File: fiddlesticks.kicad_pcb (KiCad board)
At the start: 4 copper layers, 50 x 50 mm, 99 parts, among them J1 Conn_01x02_Pin, J2 Conn_01x04_Pin, J3 Conn_01x04, J4 USB_C_Receptacle_USB2.0_16P, J5 Conn_02x04_Counter_Clockwise, J6 Conn_01x05_Pin, M1 Motor_DC, M2 Motor_DC, M3 Motor_DC, M4 Motor_DC, Q1 AO3400A, Q2 AO3400A, Q3 AO3400A, Q4 AO3400A, SW1 SW_Push, SW2 SW_Push, U1 MCP1640Bx-xCHY, U2 STM32F411CEUx, U3 SPX3819M5-L-3-3, U4 USBLC6-2SC6, U5 ICM-45605, Y1 8MHz 12pF

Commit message: routed some more things
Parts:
- removed C28: 10u, Capacitor_SMD:C_0805_2012Metric_Pad1.18x1.45mm_HandSolder
- C30, C32, C33, D10, D11, D13: moved to B.Cu
- moved D13 91.1 mm to (145.5, 125.5), turned to 90 degrees
- moved Y1 84.3 mm to (118.0, 103.0), turned to 90 degrees
- moved C11 83.4 mm to (121.0, 102.8), turned to 90 degrees
- moved C13 83.1 mm to (121.0, 106.6), turned to 90 degrees
- moved D11 82.1 mm to (134.0, 125.5), turned to 90 degrees
- moved C26 77.4 mm to (138.5, 112.5), turned to 90 degrees
- moved C33 76.5 mm to (138.5, 125.0), turned to 90 degrees
- moved D10 73.6 mm to (122.0, 125.5), turned to 90 degrees
- moved C32 66.9 mm to (127.0, 125.0), turned to 90 degrees
- moved C27 66.9 mm to (136.5, 112.6), turned to 90 degrees
- moved C29 65.3 mm to (134.6, 115.5)
- moved U5 59.4 mm to (133.8, 113.1)
- moved C30 59.3 mm to (115.0, 125.0), turned to 90 degrees
- moved R17 55.9 mm to (133.1, 109.7)
- moved C34 52.0 mm to (123.5, 118.5), turned to 90 degrees
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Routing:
- net GND: track 8.46 -> 52.3 mm, vias 17 -> 33
- net VBAT: track 13.0 -> 36.3 mm, vias 6 -> 3
- net /motor_driver_imu/PWM1: track 0.00 -> 21.2 mm, vias 0 -> 1
- net Net-(D11-A): track 0.00 -> 10.8 mm
- net Net-(D13-A): track 0.00 -> 10.7 mm
- net Net-(D10-A): track 0.00 -> 10.7 mm
- net /motor_driver_imu/PWM2: track 0.00 -> 9.72 mm, vias 0 -> 1
- net /motor_driver_imu/PWM3: track 0.00 -> 8.86 mm, vias 0 -> 1
- net /HSE_IN: track 0.00 -> 8.32 mm
- net /IMU_MOSI: track 0.00 -> 7.31 mm
- net /IMU_MISO: track 0.00 -> 7.06 mm, vias 0 -> 2
- net /IMU_CS: track 0.00 -> 6.82 mm, vias 0 -> 2
- net /HSE_OUT: track 0.00 -> 6.05 mm
- net +3.3V: track 0.00 -> 5.35 mm
- net Net-(Q1-G): track 0.43 -> 4.25 mm
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
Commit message: finished routing
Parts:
- removed C23, C6, C7, C8, C9: 10u, Capacitor_SMD:C_0805_2012Metric_Pad1.18x1.45mm_HandSolder
- removed J3: Conn_01x04, Connector_Wire:SolderWire-6sqmm_1x04_P14mm_D3.5mm_OD7mm
- removed J5: Conn_02x04_Counter_Clockwise, Connector_PinSocket_2.54mm:PinSocket_2x04_P2.54mm_Vertical
- removed U5: ICM-45605, IMU:XDCR_ICM-45605
- added MT1: ICM-42670-P, IMU:XDCR_ICM-42670-P, F.Cu at (135.0, 119.0)
- added TP5: TestPoint, TestPoint:TestPoint_Pad_1.5x1.5mm, F.Cu at (107.5, 100.5)
- added TP6: TestPoint, TestPoint:TestPoint_Pad_1.5x1.5mm, B.Cu at (107.5, 100.5)
- added TP7: TestPoint, TestPoint:TestPoint_Pad_1.5x1.5mm, F.Cu at (145.0, 118.0)
- C10, C12, C14, C15, C16, C18, C19, C24, C25, C4, D15, D16, D6, D7, D8, FB1, L1, R1, R12, R2, R3, R4, R5, R6, R7, R9, TP1, TP2, U1, U3: moved to B.Cu
- C21: value 100n -> 10uF; footprint Capacitor_SMD:C_0603_1608Metric_Pad1.08x0.95mm_HandSolder -> Capacitor_SMD:C_0805_2012Metric_Pad1.18x1.45mm_HandSolder; moved to B.Cu
- C22: value 100n -> 100nF; moved to B.Cu
- C26: value 10u -> 2.2uF
- C29: value 100n -> 10nF
- J4: value USB_C_Receptacle_USB2.0_16P -> TYPE-C-31-M-12; footprint Connector_USB:USB_C_Receptacle_Palconn_UTC16-G -> USB_CUSTOM:HRO_TYPE-C-31-M-12
- SW1: footprint coolswitch:XUNPU TS-1088-AR02016 -> coolswitch:SW_TS-1088-AR02016; moved to B.Cu
- SW2: footprint coolswitch:XUNPU TS-1088-AR02016 -> coolswitch:SW_TS-1088-AR02016
- moved SW2 100.7 mm to (138.1, 96.0), turned to 180 degrees
- moved C2 93.7 mm to (132.6, 100.0)
- moved D2 91.6 mm to (137.8, 93.5)
- moved C5 90.9 mm to (130.0, 111.6), turned to -90 degrees
- moved C3 84.7 mm to (123.4, 99.5), turned to 180 degrees
- moved C4 84.0 mm to (122.5, 100.9), turned to 90 degrees
- moved C10 83.8 mm to (122.9, 113.0)
- moved C16 82.7 mm to (126.1, 111.5), turned to 180 degrees
- moved R2 82.5 mm to (129.0, 96.1), turned to 90 degrees
- moved C25 81.1 mm to (123.5, 105.4), turned to 90 degrees
- moved D3 79.3 mm to (131.3, 124.5)
- moved D9 77.3 mm to (142.0, 115.4), turned to 90 degrees
- moved R1 77.1 mm to (124.9, 109.0), turned to 180 degrees
- moved R6 76.1 mm to (123.6, 114.5)
- moved R9 75.5 mm to (127.4, 105.1), turned to -90 degrees
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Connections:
- R17 pad 1: /IMU_SCK -> Net-(D12-K)
- R17 pad 2: Net-(D12-K) -> /IMU_SCK
- U2 pad 42: TIM4_CH1 -> unconnected-(U2-PB6-Pad42)
- U2 pad 43: TIM4_CH2 -> unconnected-(U2-PB7-Pad43)
- U2 pad 45: TIM4_CH3 -> unconnected-(U2-PB8-Pad45)
- U2 pad 46: TIM4_CH4 -> unconnected-(U2-PB9-Pad46)
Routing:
- net GND: track 52.3 -> 129.1 mm, vias 33 -> 64
- net /RC_RX: track 0.00 -> 60.4 mm, vias 0 -> 1
- net VBUS: track 15.2 -> 72.5 mm, vias 0 -> 1
- net /SWCLK: track 0.00 -> 53.4 mm, vias 0 -> 2
- net Net-(D6-K): track 0.00 -> 51.6 mm, vias 0 -> 1
- net +3.3V: track 5.35 -> 55.8 mm, vias 0 -> 12
- net /RC_TX: track 0.00 -> 49.0 mm, vias 0 -> 1
- net /motor_driver_imu/PWM2: track 9.72 -> 43.5 mm, vias 1 -> 3
- net /motor_driver_imu/PWM1: track 21.2 -> 53.0 mm, vias 1 -> 3
- net VBAT: track 36.3 -> 68.0 mm, vias 3 -> 5
- net /SWDIO: track 0.00 -> 31.6 mm, vias 0 -> 2
- net /motor_driver_imu/PWM4: track 0.00 -> 30.2 mm, vias 0 -> 1
- net +5V: track 0.00 -> 25.2 mm, vias 0 -> 3
- net VSYS: track 0.00 -> 22.4 mm, vias 0 -> 2
- net /mcu_boot0: track 0.00 -> 19.0 mm, vias 0 -> 2
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- added copper zone on In2.Cu, net +3.3V
- added copper zone on B.Cu, net GND
- added copper zone on In2.Cu, net VSYS
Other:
- board text added: "+ -"
- board text added: "3.3V"
- board text added: "5V"
- board text added: "BOOT0"
- board text added: "FIDDLESTICKS"
- board text added: "GND"
- board text added: "GND|3v3|5|RX|TX"
- board text added: "NRST"
- board text added: "RHR"
- board text added: "RX"
- board text added: "V0"
- board text added: "VBUS"
- board text added: "VBUS|VBAT"
- board text added: "VSYS"
- board text added: "X"
- board text added: "Y"

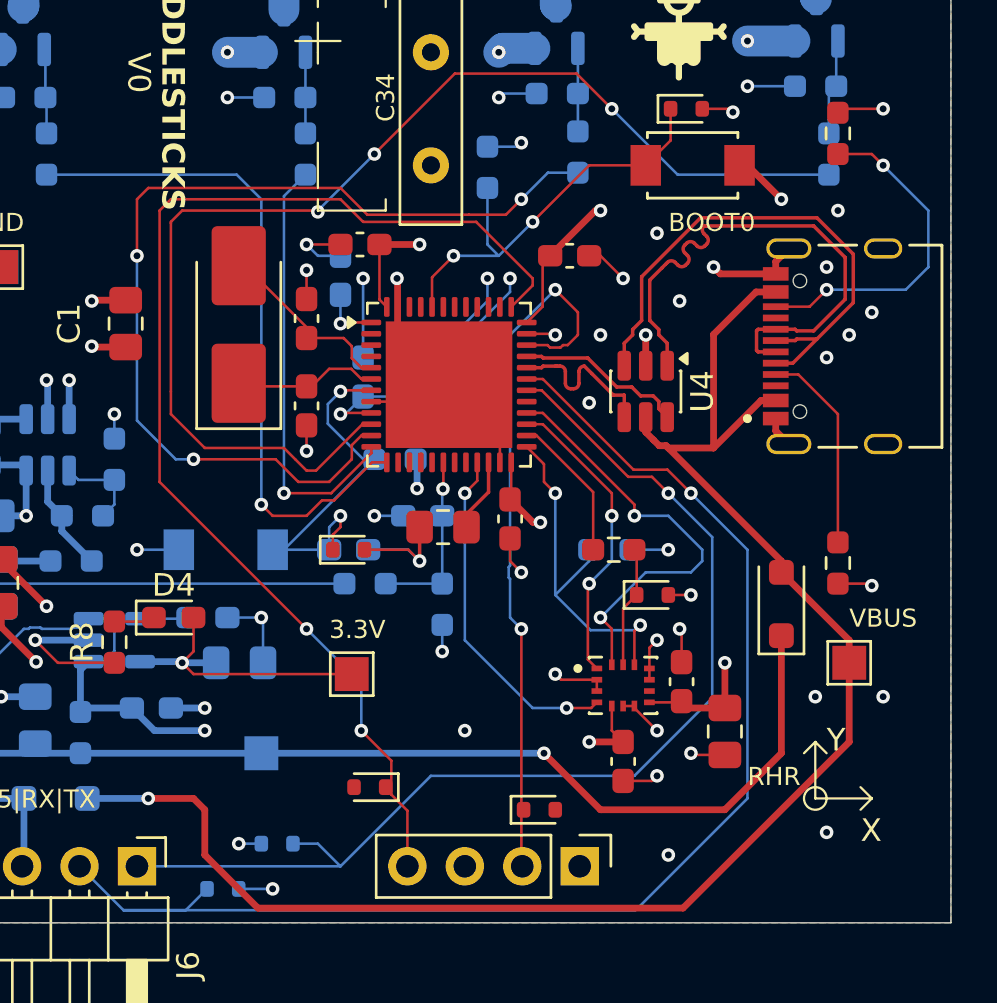
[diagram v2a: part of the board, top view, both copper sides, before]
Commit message: fixed usb routing, and esd/pull ups/pull downs placement
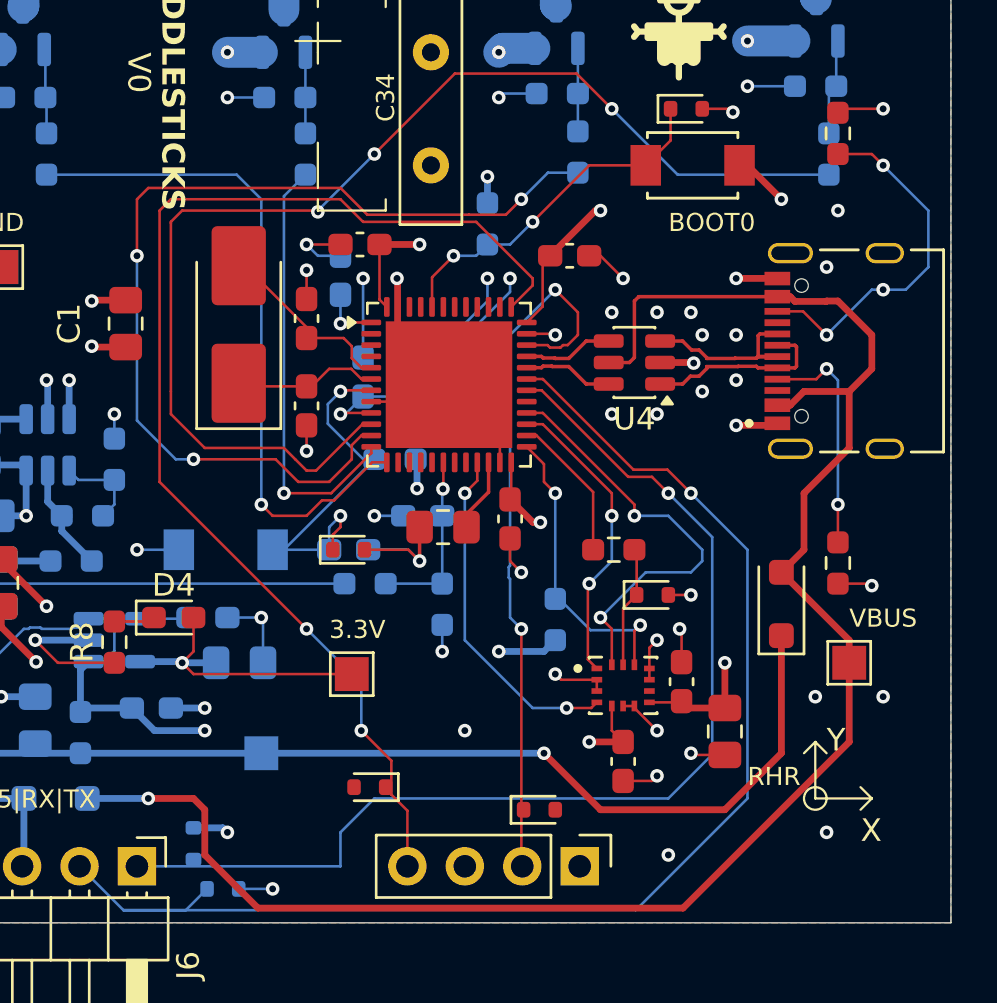
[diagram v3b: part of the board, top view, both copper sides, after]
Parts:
- moved R12 3.92 mm to (132.0, 116.1), turned to -90 degrees
- moved D15 3.70 mm to (116.0, 126.0), turned to 90 degrees
- moved R2 2.50 mm to (129.0, 98.6)
- moved U4 1.37 mm to (135.5, 104.7), turned to 180 degrees
- moved J4 0.22 mm to (146.6, 104.2)
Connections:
- U4 pad 1: /DIN+ -> /DIN-
- U4 pad 3: /DIN- -> /DIN+
- U4 pad 4: /USB_FS_D- -> /USB_FS_D+
- U4 pad 6: /USB_FS_D+ -> /USB_FS_D-
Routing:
- net /DIN+: track 24.2 -> 8.20 mm
- net /DIN-: track 23.9 -> 8.20 mm
- net VBUS: track 72.5 -> 79.3 mm
- net /USB_FS_D+: track 7.51 -> 3.98 mm
- net /USB_FS_D-: track 7.40 -> 3.98 mm
- net /mcu_boot0: track 19.0 -> 15.8 mm
- net /IMU_CS: track 16.0 -> 13.4 mm
- net GND: track 129.1 -> 127.5 mm, vias 64 -> 67
- net Net-(J4-CC1): track 9.15 -> 10.3 mm, vias 0 -> 2
- net +3.3V: track 55.8 -> 56.8 mm
- net Net-(J4-CC2): track 15.0 -> 15.9 mm, vias 2 -> 3

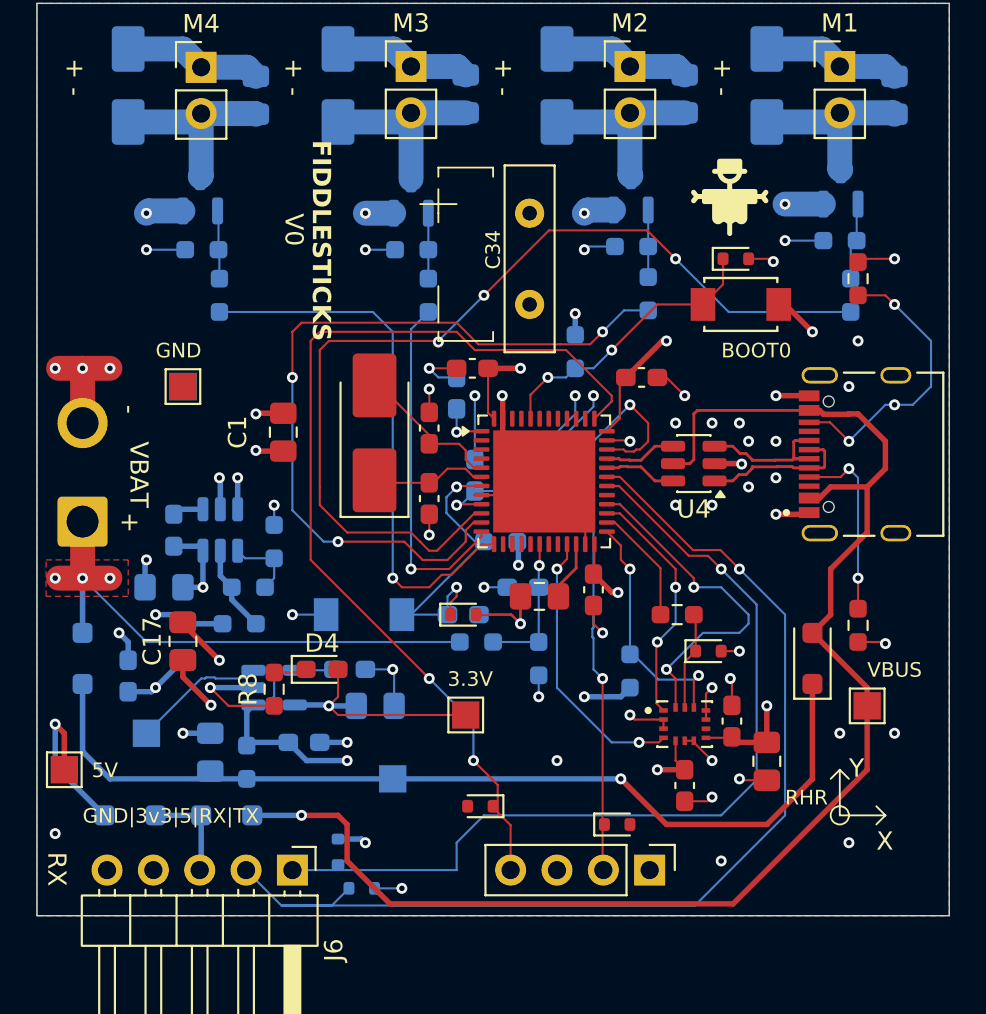
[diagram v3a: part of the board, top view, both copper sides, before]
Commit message: added vias under MCU, added silk screen for SWD
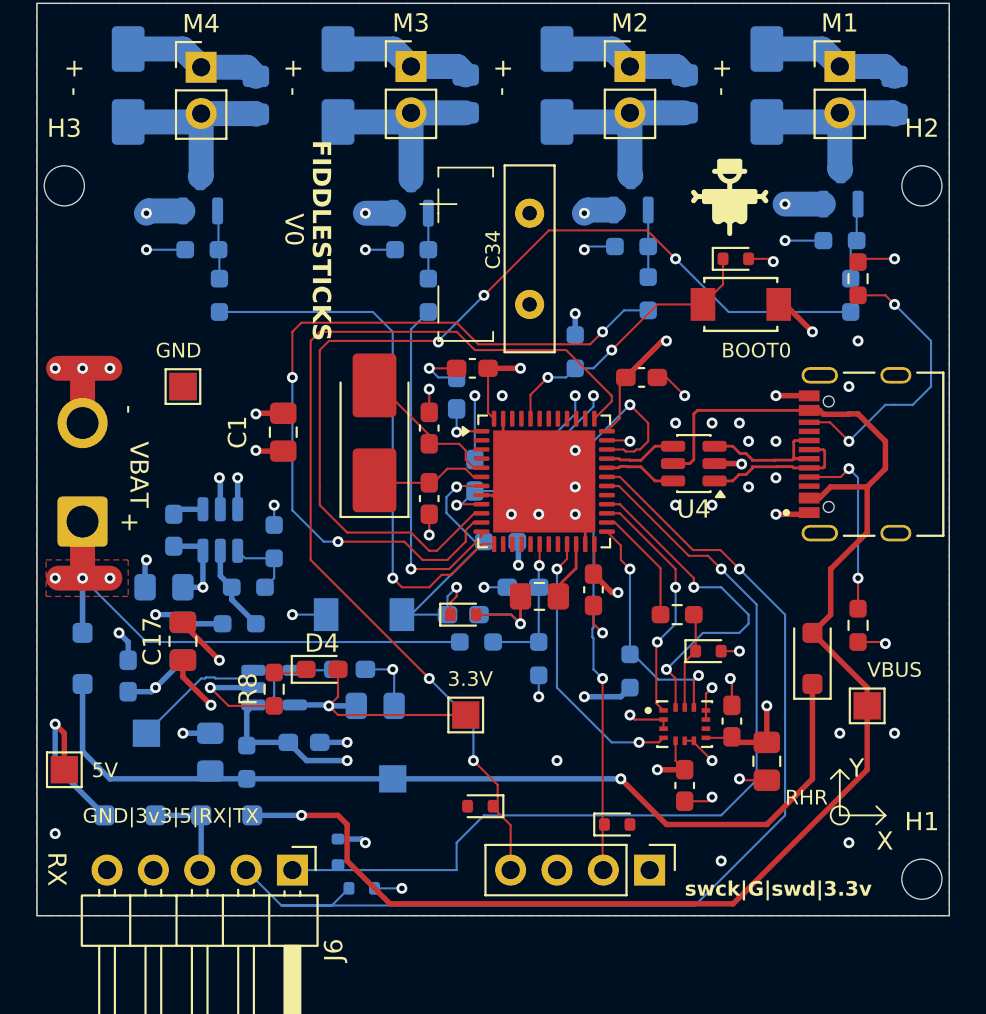
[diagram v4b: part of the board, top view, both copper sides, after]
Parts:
- added H1: MountingHole, MountingHole:MountingHole_2.2mm_M2, F.Cu at (148.0, 127.5)
- added H2: MountingHole, MountingHole:MountingHole_2.2mm_M2, F.Cu at (148.0, 89.5)
- added H3: MountingHole, MountingHole:MountingHole_2.2mm_M2, F.Cu at (101.0, 89.5)
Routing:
- net GND: track 127.5 -> 132.6 mm, vias 67 -> 72
- net Net-(J4-CC2): vias 3 -> 2
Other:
- board text added: "swck|G|swd|3.3v"

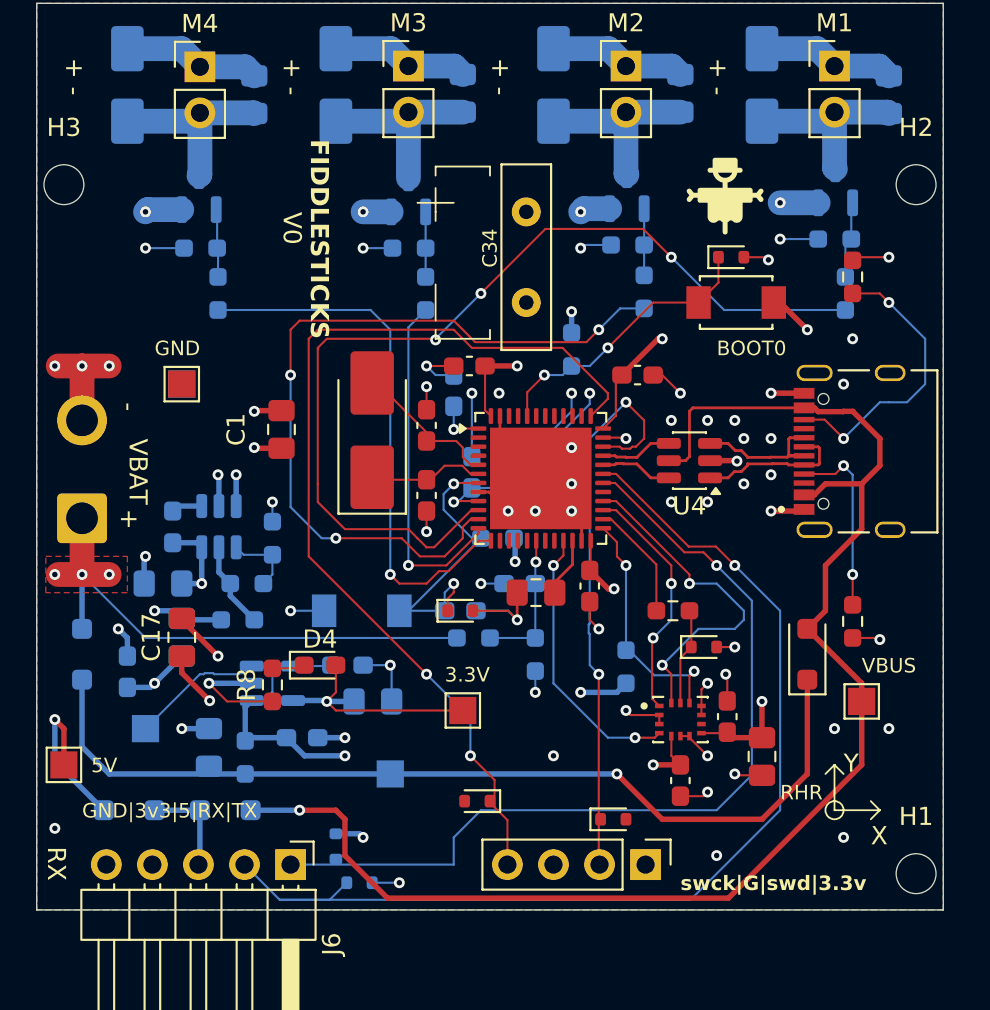
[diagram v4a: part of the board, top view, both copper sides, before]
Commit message: fixed some more routing
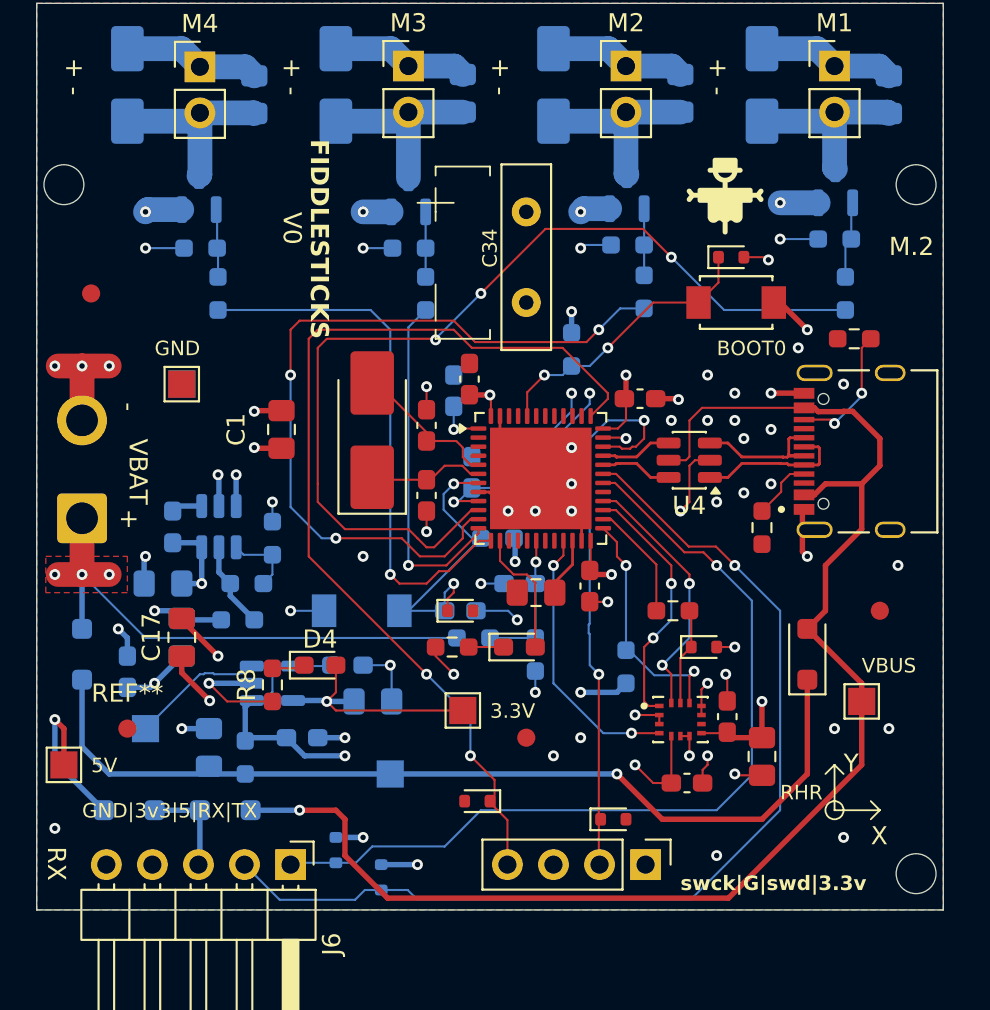
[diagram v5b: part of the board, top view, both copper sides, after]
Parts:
- added D14: GREEN, LED_SMD:LED_0603_1608Metric_Pad1.05x0.95mm_HandSolder, F.Cu at (126.1, 115.0)
- added R22: 1k, Resistor_SMD:R_0603_1608Metric_Pad0.98x0.95mm_HandSolder, F.Cu at (122.4, 115.0)
- added REF**: Fiducial_1mm_Mask2mm, Fiducial:Fiducial_1mm_Mask2mm, F.Cu at (146.0, 113.0)
- added REF**: Fiducial_1mm_Mask2mm, Fiducial:Fiducial_1mm_Mask2mm, F.Cu at (104.5, 119.5)
- added REF**: Fiducial_1mm_Mask2mm, Fiducial:Fiducial_1mm_Mask2mm, F.Cu at (102.5, 95.5)
- added REF**: Fiducial_1mm_Mask2mm, Fiducial:Fiducial_1mm_Mask2mm, F.Cu at (126.5, 120.0)
- moved R10 7.20 mm to (139.5, 108.4)
- moved R11 3.41 mm to (144.6, 98.0), turned to 180 degrees
- moved C2 1.31 mm to (132.8, 101.3)
- moved D16 1.24 mm to (118.5, 127.7), turned to 90 degrees
- moved C3 0.72 mm to (123.4, 100.2), turned to 90 degrees
- moved C29 0.39 mm to (135.4, 122.5), turned to 0 degrees
- moved D15 0.20 mm to (116.0, 126.2)
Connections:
- U2 pad 14: /NRF_NCS -> /DBG_LED
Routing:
- net GND: track 132.6 -> 121.4 mm
- net Net-(J4-CC2): track 15.9 -> 7.26 mm
- net /DBG_LED: track 0.00 -> 7.10 mm
- net Net-(J4-CC1): track 10.3 -> 3.46 mm, vias 2 -> 0
- net /IMU_MOSI: track 18.9 -> 14.4 mm
- net /RC_RX: track 60.4 -> 56.7 mm
- net +3.3V: track 56.8 -> 53.3 mm
- net Net-(D14-K): track 0.00 -> 1.92 mm
- net /RC_TX: track 48.9 -> 48.0 mm
- net /SWDIO: track 31.6 -> 30.7 mm
- net /IMU_MISO: track 13.4 -> 14.1 mm
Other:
- board text added: "M.2"
